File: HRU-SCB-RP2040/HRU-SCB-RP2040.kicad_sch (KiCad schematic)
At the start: 5 parts, among them U1 RaspberryPi_Pico_W

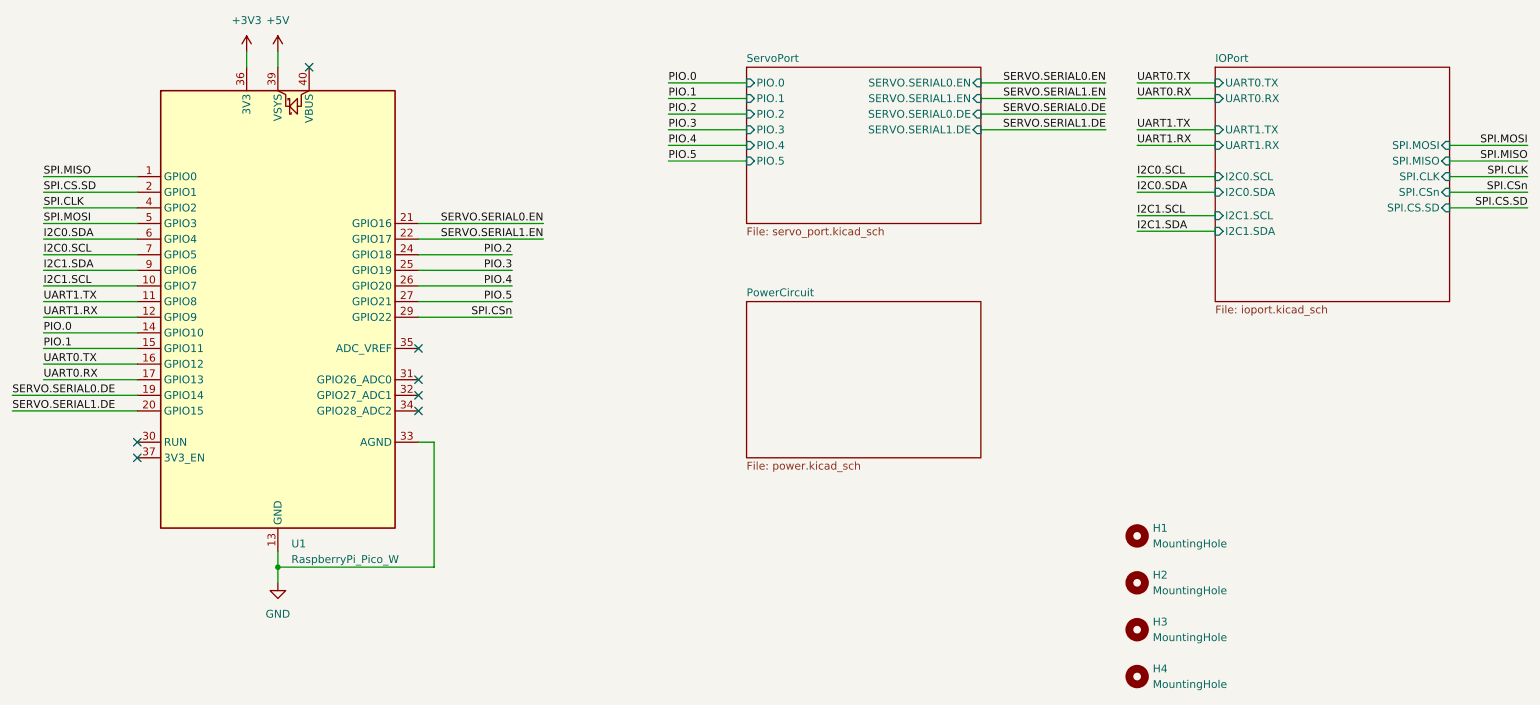
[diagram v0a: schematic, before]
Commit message: Delete PWM circuit
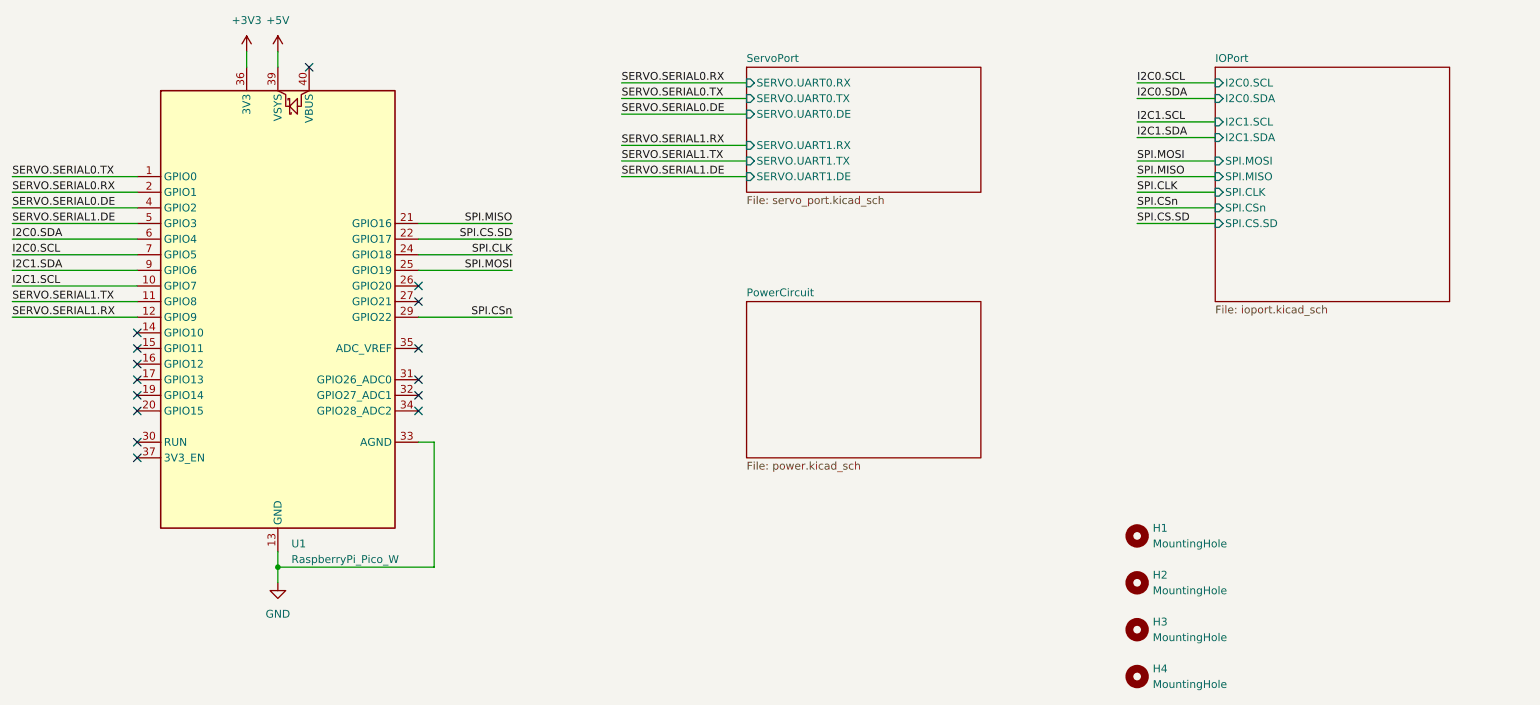
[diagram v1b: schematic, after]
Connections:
- net PIO.2 is gone; now on net SPI.CLK: U1.24 (GPIO18)
- net PIO.3 is gone; now on net SPI.MOSI: U1.25 (GPIO19)
- net SERVO.SERIAL0.EN is gone; now on net SPI.MISO: U1.21 (GPIO16)
- net SERVO.SERIAL1.EN is gone; now on net SPI.CS.SD: U1.22 (GPIO17)
- net SERVO.SERIAL0.DE: now also U1.4 (GPIO2); no longer U1.19 (GPIO14)
- net SERVO.SERIAL1.DE: now also U1.5 (GPIO3); no longer U1.20 (GPIO15)
- net SPI.CLK: no longer U1.4 (GPIO2)
- net SPI.CS.SD: no longer U1.2 (GPIO1)
- net SPI.MISO: no longer U1.1 (GPIO0)
- net SPI.MOSI: no longer U1.5 (GPIO3)
- net PIO.0: no longer names the net of U1.14 (GPIO10)
- net PIO.1: no longer names the net of U1.15 (GPIO11)
- net PIO.4: no longer names the net of U1.26 (GPIO20)
- net PIO.5: no longer names the net of U1.27 (GPIO21)
- net UART0.RX: no longer names the net of U1.17 (GPIO13)
- net UART0.TX: no longer names the net of U1.16 (GPIO12)
- net UART1.RX renamed SERVO.SERIAL1.RX
- net UART1.TX renamed SERVO.SERIAL1.TX
- new net SERVO.SERIAL0.RX: U1.2 (GPIO1)
- new net SERVO.SERIAL0.TX: U1.1 (GPIO0)
- no-connect marks 7 -> 15
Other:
- sheet IOPort ports: added none; removed UART0.RX, UART0.TX, UART1.RX, UART1.TX
- sheet ServoPort ports: added SERVO.UART0.DE, SERVO.UART0.RX, SERVO.UART0.TX, SERVO.UART1.DE, SERVO.UART1.RX, SERVO.UART1.TX; removed PIO.0, PIO.1, PIO.2, PIO.3, PIO.4, PIO.5, SERVO.SERIAL0.DE, SERVO.SERIAL0.EN, SERVO.SERIAL1.DE, SERVO.SERIAL1.EN

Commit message: Update design for hand soldering friendly
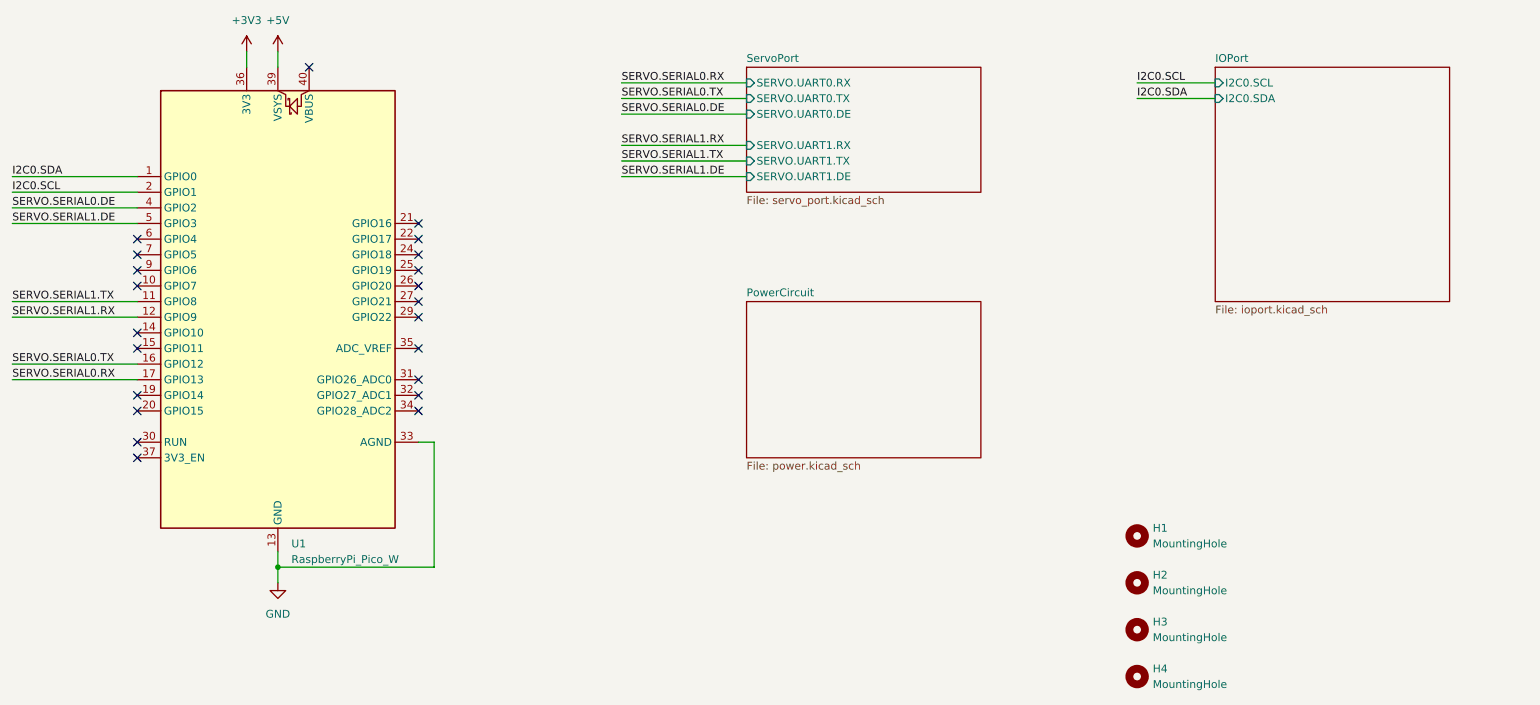
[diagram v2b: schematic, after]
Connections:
- net I2C0.SCL: now also U1.2 (GPIO1); no longer U1.7 (GPIO5)
- net I2C0.SDA: now also U1.1 (GPIO0); no longer U1.6 (GPIO4)
- net SERVO.SERIAL0.RX: now also U1.17 (GPIO13); no longer U1.2 (GPIO1)
- net SERVO.SERIAL0.TX: now also U1.16 (GPIO12); no longer U1.1 (GPIO0)
- net I2C1.SCL: no longer names the net of U1.10 (GPIO7)
- net I2C1.SDA: no longer names the net of U1.9 (GPIO6)
- net SPI.CLK: no longer names the net of U1.24 (GPIO18)
- net SPI.CS.SD: no longer names the net of U1.22 (GPIO17)
- net SPI.CSn: no longer names the net of U1.29 (GPIO22)
- net SPI.MISO: no longer names the net of U1.21 (GPIO16)
- net SPI.MOSI: no longer names the net of U1.25 (GPIO19)
- no-connect marks 15 -> 22
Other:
- sheet IOPort ports: added none; removed I2C1.SCL, I2C1.SDA, SPI.CLK, SPI.CS.SD, SPI.CSn, SPI.MISO, SPI.MOSI

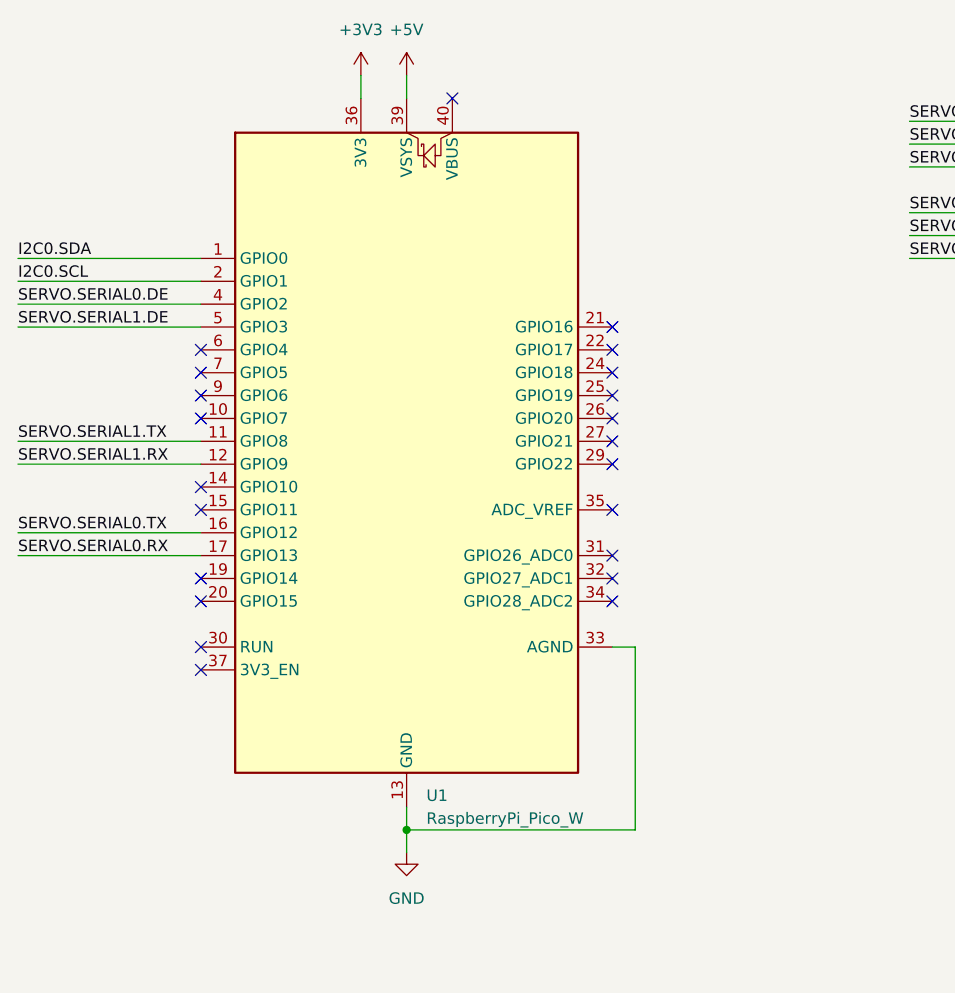
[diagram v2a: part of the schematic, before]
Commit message: Update DCDC for DIP soldering
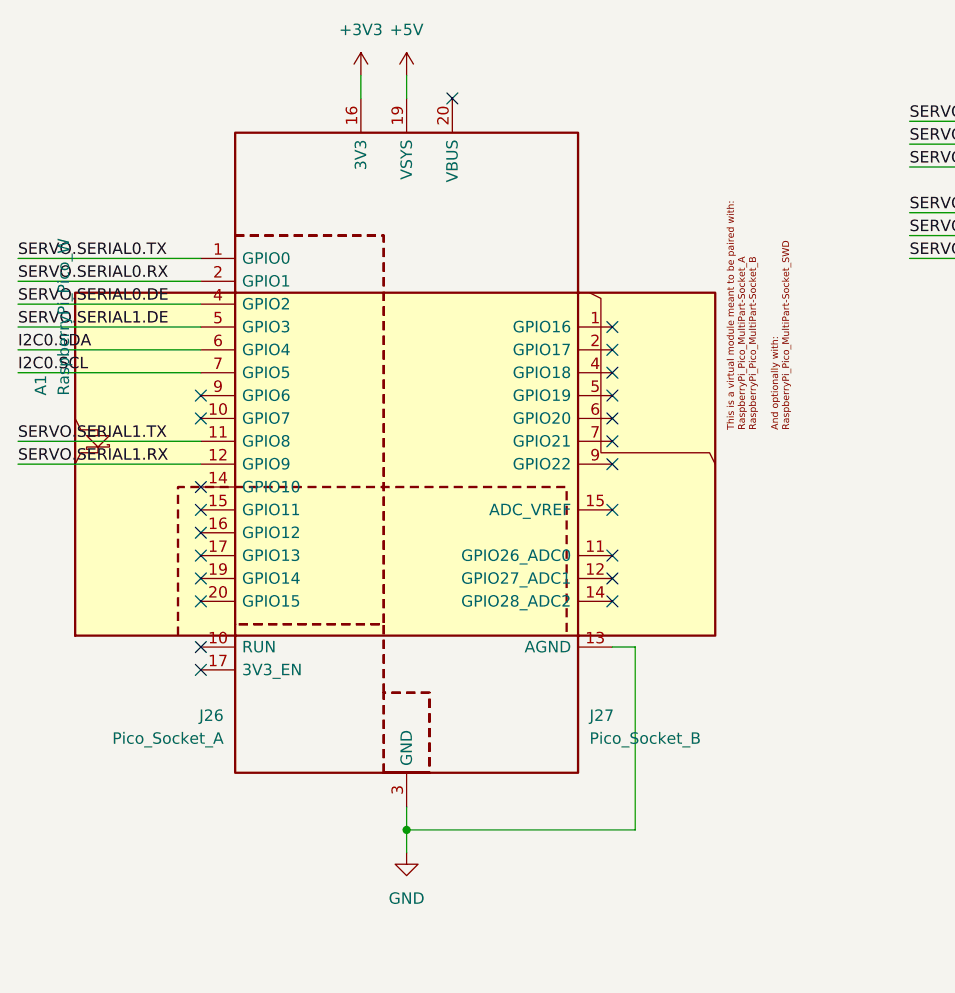
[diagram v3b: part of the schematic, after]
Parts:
- removed U1: RaspberryPi_Pico_W, Module_RaspberryPi_Pico:RaspberryPi_Pico_Common_THT, symbol MCU_Module_RaspberryPi_Pico:RaspberryPi_Pico_W
- added A1: RaspberryPi_Pico_W, Module_RaspberryPi_Pico:RaspberryPi_Pico_W_Virtual, symbol MCU_Module_RaspberryPi_Pico:RaspberryPi_Pico_W_MultiPart-Module
- added J26: Pico_Socket_A, Module_RaspberryPi_Pico:RaspberryPi_Pico_PinSocket_1x20_P2.54mm_Vertical, symbol MCU_Module_RaspberryPi_Pico:RaspberryPi_Pico_MultiPart-Socket_A
- added J27: Pico_Socket_B, Module_RaspberryPi_Pico:RaspberryPi_Pico_PinSocket_1x20_P2.54mm_Vertical, symbol MCU_Module_RaspberryPi_Pico:RaspberryPi_Pico_MultiPart-Socket_B
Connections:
- net +3V3: now also J27.16 (3V3)
- net +5V: now also J27.19 (VSYS)
- net GND: now also J26.13 (GND), J26.18 (GND), J26.3 (GND), J26.8 (GND), J27.13 (AGND), J27.18 (GND), J27.3 (GND), J27.8 (GND)
- net I2C0.SCL: now also J26.7 (GPIO5)
- net I2C0.SDA: now also J26.6 (GPIO4)
- net SERVO.SERIAL0.DE: now also J26.4 (GPIO2)
- net SERVO.SERIAL0.RX: now also J26.2 (GPIO1)
- net SERVO.SERIAL0.TX: now also J26.1 (GPIO0)
- net SERVO.SERIAL1.DE: now also J26.5 (GPIO3)
- net SERVO.SERIAL1.RX: now also J26.12 (GPIO9)
- net SERVO.SERIAL1.TX: now also J26.11 (GPIO8)
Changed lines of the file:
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@@
 	)
 	(no_connect
-		(at 53.34 58.42)
-	)
-	(no_connect
 		(at 99.06 76.2)
 	)
@@
 	)
 	(no_connect
-		(at 53.34 81.28)
+		(at 53.34 58.42)
 	)
 	(no_connect
-		(at 53.34 53.34)
+		(at 53.34 81.28)
 	)
 	(no_connect
@@
 	)
 	(no_connect
-		(at 53.34 60.96)
-	)
-	(no_connect
-		(at 53.34 55.88)
+		(at 53.34 88.9)
 	)
 	(no_connect
-		(at 53.34 88.9)
+		(at 53.34 60.96)
 	)
 	(no_connect
@@
 	)
 	(no_connect
+		(at 53.34 73.66)
+	)
+	(no_connect
 		(at 99.06 53.34)
 	)
@@
 	)
 	(no_connect
+		(at 53.34 76.2)
+	)
+	(no_connect
 		(at 99.06 71.12)
 	)
@@
 	(wire
 		(pts
-			(xy 53.34 76.2) (xy 33.02 76.2)
+			(xy 53.34 45.72) (xy 33.02 45.72)
 		)
 		(stroke
@@
 	(wire
 		(pts
-			(xy 53.34 45.72) (xy 33.02 45.72)
+			(xy 53.34 55.88) (xy 33.02 55.88)
 		)
 		(stroke
@@
 	(wire
 		(pts
-			(xy 53.34 43.18) (xy 33.02 43.18)
+			(xy 53.34 53.34) (xy 33.02 53.34)
 		)
 		(stroke
@@
 	(wire
 		(pts
-			(xy 53.34 73.66) (xy 33.02 73.66)
+			(xy 53.34 43.18) (xy 33.02 43.18)
 		)
 		(stroke
@@
 	)
 	(label "SERVO.SERIAL0.RX"
-		(at 33.02 76.2 0)
+		(at 33.02 45.72 0)
 		(fields_autoplaced yes)
 		(effects
@@
 	)
 	(label "I2C0.SDA"
-		(at 33.02 43.18 0)
+		(at 33.02 53.34 0)
 		(fields_autoplaced yes)
 		(effects
@@
 	)
 	(label "SERVO.SERIAL0.TX"
-		(at 33.02 73.66 0)
+		(at 33.02 43.18 0)
 		(fields_autoplaced yes)
 		(effects
@@
 	)
 	(label "I2C0.SCL"
-		(at 33.02 45.72 0)
+		(at 33.02 55.88 0)
 		(fields_autoplaced yes)
 		(effects
@@
 	)
 	(symbol
-		(lib_id "MCU_Module_RaspberryPi_Pico:RaspberryPi_Pico_W")
-		(at 76.2 66.04 0)
+		(lib_id "MCU_Module_RaspberryPi_Pico:RaspberryPi_Pico_W_MultiPart-Module")
+		(at 76.2 66.04 90)
 		(unit 1)
 		(exclude_from_sim no)
@@
 		(dnp no)
 		(fields_autoplaced yes)
-		(property "Reference" "U1"
-			(at 78.3941 102.87 0)
+		(property "Reference" "A1"
+			(at 35.56 58.42 0)
+			(do_not_autoplace yes)
 			(effects
 				(font
@@
 		)
 		(property "Value" "RaspberryPi_Pico_W"
-			(at 78.3941 105.41 0)
+			(at 38.1 58.42 0)
+			(do_not_autoplace yes)
 			(effects
 				(font
@@
 			)
 		)
-		(property "Footprint" "Module_RaspberryPi_Pico:RaspberryPi_Pico_Common_THT"
-			(at 76.2 115.57 0)
+		(property "Footprint" "Module_RaspberryPi_Pico:RaspberryPi_Pico_W_Virtual"
+			(at 125.73 66.04 0)
 			(effects
 				(font
@@
 		)
 		(property "Datasheet" "https://datasheets.raspberrypi.com/picow/pico-w-datasheet.pdf"
-			(at 76.2 118.11 0)
+			(at 128.27 66.04 0)
 			(effects
 				(font
@@
 			)
 		)
-		(property "Description" ""
-			(at 76.2 66.04 0)
+		(property "Description" "Versatile and inexpensive wireless microcontroller module (virtual representation) powered by RP2040 dual-core Arm Cortex-M0+ processor up to 133 MHz, 264kB SRAM, 2MB QSPI flash, Infineon CYW43439 2.4GHz 802.11n wireless LAN"
+			(at 130.81 66.04 0)
 			(effects
 				(font
@@
 			)
 		)
-		(pin "1"
-		)
-		(pin "10"
-		)
-		(pin "11"
-		)
-		(pin "12"
-		)
-		(pin "13"
-		)
-		(pin "14"
-		)
-		(pin "15"
-		)
-		(pin "16"
-		)
-		(pin "17"
-		)
-		(pin "18"
-		)
-		(pin "19"
-		)
-		(pin "2"
-		)
-		(pin "20"
-		)
-		(pin "21"
-		)
-		(pin "22"
-		)
-		(pin "23"
-		)
-		(pin "24"
-		)
-		(pin "25"
-		)
-		(pin "26"
-		)
-		(pin "27"
-		)
-		(pin "28"
-		)
-		(pin "29"
-		)
-		(pin "3"
-		)
-		(pin "30"
-		)
-		(pin "31"
-		)
-		(pin "32"
-		)
-		(pin "33"
-		)
-		(pin "34"
-		)
-		(pin "35"
-		)
-		(pin "36"
-		)
-		(pin "37"
-		)
-		(pin "38"
-		)
-		(pin "39"
-		)
-		(pin "4"
-		)
-		(pin "40"
-		)
-		(pin "5"
-		)
-		(pin "6"
-		)
-		(pin "7"
-		)
-		(pin "8"
-		)
-		(pin "9"
-		)
 		(instances
-			(project "HRU-SCB-RP2040"
+			(project ""
 				(path "/22d57d1f-fa00-4148-a62a-8eb596ebbd21"
-					(reference "U1")
+					(reference "A1")
 					(unit 1)
 				)
@@
 	)
 	(symbol
+		(lib_id "MCU_Module_RaspberryPi_Pico:RaspberryPi_Pico_MultiPart-Socket_B")
+		(at 76.2 66.04 0)
+		(unit 1)
+		(exclude_from_sim no)
+		(in_bom yes)
+		(on_board yes)
+		(dnp no)
+		(fields_autoplaced yes)
+		(property "Reference" "J27"
+			(at 96.52 93.98 0)
+			(do_not_autoplace yes)
+			(effects
+				(font
+					(size 1.27 1.27)
+				)
+				(justify left)
+			)
+		)
+		(property "Value" "Pico_Socket_B"
+			(at 96.52 96.52 0)
+			(do_not_autoplace yes)
+			(effects
+				(font
+					(size 1.27 1.27)
+				)
+				(justify left)
+			)
+		)
+		(property "Footprint" "Module_RaspberryPi_Pico:RaspberryPi_Pico_PinSocket_1x20_P2.54mm_Vertical"
+			(at 76.2 115.57 0)
+			(effects
+				(font
+					(size 1.27 1.27)
+				)
+				(hide yes)
+			)
+		)
+		(property "Datasheet" "https://datasheets.raspberrypi.com/pico/pico-datasheet.pdf"
+			(at 76.2 118.11 0)
+			(effects
+				(font
+					(size 1.27 1.27)
+				)
+				(hide yes)
+			)
+		)
+		(property "Description" "One of two 1x20 headers for connecting a Raspberry Pi Pico, with the Pico's specific pins and capabilities implemented, single row, 01x20"
+			(at 76.2 120.65 0)
+			(effects
+				(font
+					(size 1.27 1.27)
+				)
+				(hide yes)
+			)
+		)
+		(pin "13"
+		)
+		(pin "1"
+		)
+		(pin "15"
+		)
+		(pin "5"
+		)
+		(pin "18"
+		)
+		(pin "12"
+		)
+		(pin "20"
+		)
+		(pin "9"
+		)
+		(pin "3"
+		)
+		(pin "4"
+		)
+		(pin "11"
+		)
+		(pin "2"
+		)
+		(pin "16"
+		)
+		(pin "10"
+		)
+		(pin "19"
+		)
+		(pin "8"
+		)
+		(pin "7"
+		)
+		(pin "14"
+		)
+		(pin "17"
+		)
+		(pin "6"
+		)
+		(instances
+			(project ""
+				(path "/22d57d1f-fa00-4148-a62a-8eb596ebbd21"
+					(reference "J27")
+					(unit 1)
+				)
+			)
+		)
+	)
+	(symbol
 		(lib_id "Mechanical:MountingHole")
 		(at 215.9 109.22 0)
@@
 					(unit 1)
 				)
+			)
+		)
+	)
+	(symbol
+		(lib_id "MCU_Module_RaspberryPi_Pico:RaspberryPi_Pico_MultiPart-Socket_A")
+		(at 76.2 66.04 0)
+		(unit 1)
+		(exclude_from_sim no)
+		(in_bom yes)
+		(on_board yes)
+		(dnp no)
+		(fields_autoplaced yes)
+		(property "Reference" "J26"
+			(at 55.88 93.98 0)
+			(do_not_autoplace yes)
+			(effects
+				(font
+					(size 1.27 1.27)
+				)
+				(justify right)
+			)
+		)
+		(property "Value" "Pico_Socket_A"
+			(at 55.88 96.52 0)
+			(do_not_autoplace yes)
+			(effects
+				(font
+					(size 1.27 1.27)
+				)
+				(justify right)
+			)
+		)
+		(property "Footprint" "Module_RaspberryPi_Pico:RaspberryPi_Pico_PinSocket_1x20_P2.54mm_Vertical"
+			(at 76.2 115.57 0)
+			(effects
+				(font
+					(size 1.27 1.27)
+				)
+				(hide yes)
+			)
+		)
+		(property "Datasheet" "https://datasheets.raspberrypi.com/pico/pico-datasheet.pdf"
+			(at 76.2 118.11 0)
+			(effects
+				(font
+					(size 1.27 1.27)
+				)
+				(hide yes)
+			)
+		)
+		(property "Description" "One of two 1x20 headers for connecting a Raspberry Pi Pico, with the Pico's specific pins and capabilities implemented, single row, 01x20"
+			(at 76.2 120.65 0)
+			(effects
+				(font
+					(size 1.27 1.27)
+				)
+				(hide yes)
+			)
+		)
+		(pin "15"
+		)
+		(pin "20"
+		)
+		(pin "3"
+		)
+		(pin "19"
+		)
+		(pin "2"
+		)
+		(pin "13"
+		)
+		(pin "10"
+		)
+		(pin "12"
+		)
+		(pin "7"
+		)
+		(pin "4"
+		)
+		(pin "1"
+		)
+		(pin "14"
+		)
+		(pin "5"
+		)
+		(pin "6"
+		)
+		(pin "17"
+		)
+		(pin "8"
+		)
+		(pin "9"
+		)
+		(pin "16"
+		)
+		(pin "18"
+		)
+		(pin "11"
+		)
+		(instances
+			(project ""
+				(path "/22d57d1f-fa00-4148-a62a-8eb596ebbd21"
+					(reference "J26")
+					(unit 1)
+				)
